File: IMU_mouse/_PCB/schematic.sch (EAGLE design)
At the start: 43 parts, among them IC1 REG1117, M1 WIRELESS-NRF24L01, U1 GY-521MPU6050

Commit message: IMU mouse PCB update
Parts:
- removed C2, C3, NRF: (no value), rcl:CPOL-USE2.5-5
- removed C5, C7, NRF_2: (no value), rcl:C-EUC0805
- removed D1: (no value), SparkFun-LED:LED3MM
- removed J1, J3, J4, NRF_POW1: (no value), SparkFun-Connectors:CONN_02LOCK
- removed JP2, JP3, JP4, JP5, NRF_POW: JUMPER-SMT_2_NO_SILK, SparkFun-Jumpers:JUMPER-SMT_2_NO_SILK
- removed M1: WIRELESS-NRF24L01, diy-modules:WIRELESS-NRF24L01
- removed R2, R3, R4, R5: (no value), rcl:R-US_R0805
- added JP_L, JP_R: JUMPER-SMT_2_NC_TRACE_SILK, SparkFun-Jumpers:JUMPER-SMT_2_NC_TRACE_SILK
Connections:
- removed net N$5: B1.*6, M1.CSN
- removed net N$6: M1.VCC, NRF_POW.2, NRF_POW1.2
- net 3.3V: no longer NRF.+, NRF_2.1, NRF_POW.1, NRF_POW1.1
- net 5V: now also LEFT.2, RIGHT.2; no longer LEFT.1, RIGHT.1
- net GND: no longer M1.GND, NRF.-, NRF_2.2
- net N$1: now also J2.2, JP_L.2, LEFT.1; no longer B1.12(MISO), M1.MISO
- net N$2: now also J2.1, JP_R.2, RIGHT.1; no longer B1.11(MOSI), M1.MOSI
- net N$3: now also B1.*5, JP_R.1; no longer B1.13(SCK), M1.SCK
- net N$4: now also B1.*6, JP_L.1; no longer B1.7, M1.CE
- net N$8: now also JP_SDA.2; no longer JP_SDA.1
- net N$9: now also JP_SCL.2; no longer JP_SCL.1
- net SCL: now also JP_SCL.1; no longer JP_SCL.2
- net SDA: now also JP_SDA.1; no longer JP_SDA.2
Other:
- moved on the sheet: B1, C_5V, C_5V_1, GY-521, H1, H2, H3, H4, IC1, IN, IN_2, J2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

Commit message: IMU mouse PCB
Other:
- moved on the sheet: H1, H2, H3, H4
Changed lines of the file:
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@@
 <instance part="J6" gate="G$1" x="147.32" y="38.1"/>
 <instance part="SHIELD" gate="G$1" x="157.48" y="10.16"/>
-<instance part="H1" gate="G$1" x="241.3" y="25.4"/>
-<instance part="H2" gate="G$1" x="241.3" y="20.32"/>
-<instance part="H3" gate="G$1" x="241.3" y="15.24"/>
-<instance part="H4" gate="G$1" x="241.3" y="10.16"/>
+<instance part="H1" gate="G$1" x="195.58" y="99.06"/>
+<instance part="H2" gate="G$1" x="195.58" y="93.98"/>
+<instance part="H3" gate="G$1" x="195.58" y="88.9"/>
+<instance part="H4" gate="G$1" x="195.58" y="83.82"/>
 <instance part="JP_SCL" gate="G$1" x="76.2" y="132.08"/>
 <instance part="JP_SDA" gate="G$1" x="76.2" y="124.46"/>

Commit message: update
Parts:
- removed C_5V: (no value), rcl:CPOL-USE2.5-5
- added 3.3V: (no value), SparkFun-Connectors:CONN_03
- added GY521_2: (no value), SparkFun-Connectors:CONN_08"
- added GY_3.3V: 3.3V, SparkFun-Jumpers:JUMPER-SMT_2_NO_NO-SILK
- added GY_5V_DEFAULT: 5V, SparkFun-Jumpers:JUMPER-SMT_2_NC_TRACE_SILK
- added POWER: FEMALE 2x3, SparkFun-Connectors:CONN_03X2FEMALE
- added RESET1: MOMENTARY-SWITCH-SPST-PTH-6.0MM, SparkFun-Switches:MOMENTARY-SWITCH-SPST-PTH-6.0MM
- added RESET2: 6*3.5mm, SparkFun-Switches:MOMENTARY-SWITCH-SPST-SMD-6.0X3.5MM
- IN, OUT: value (none) -> 100nF
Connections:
- new net N$5: GY521_2.1, GY_3.3V.1, GY_5V_DEFAULT.1, U1.VCC
- new net N$6: B1.RESET, RESET1.1, RESET2.1
- net 3.3V: now also 3.3V.1, 3.3V.2, 3.3V.3, GY_3.3V.2
- net 5V: now also GY_5V_DEFAULT.2, POWER.1, POWER.3, POWER.5; no longer C_5V.+, LEFT.2, RIGHT.2, U1.VCC
- net GND: now also GY521_2.2, LEFT.2, POWER.2, POWER.4, POWER.6, RESET1.2, RESET2.2, RIGHT.2; no longer C_5V.-
- net N$10: now also GY521_2.8
- net N$11: now also GY521_2.7
- net N$12: now also GY521_2.6
- net N$13: now also GY521_2.5
- net SCL: now also GY521_2.3
- net SDA: now also GY521_2.4
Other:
- moved on the sheet: GY-521, JP_SCL, JP_SDA

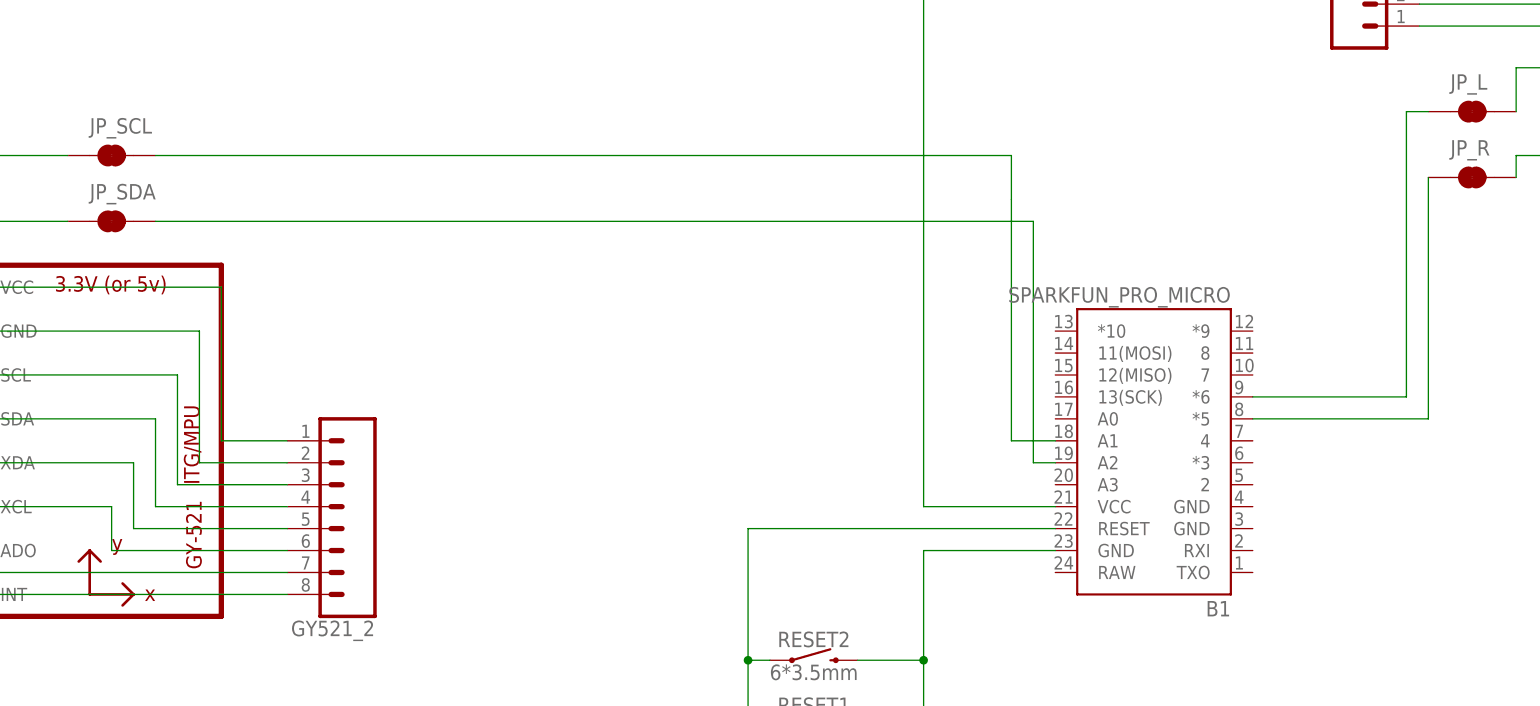
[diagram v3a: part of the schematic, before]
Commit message: IMU code, PCB update
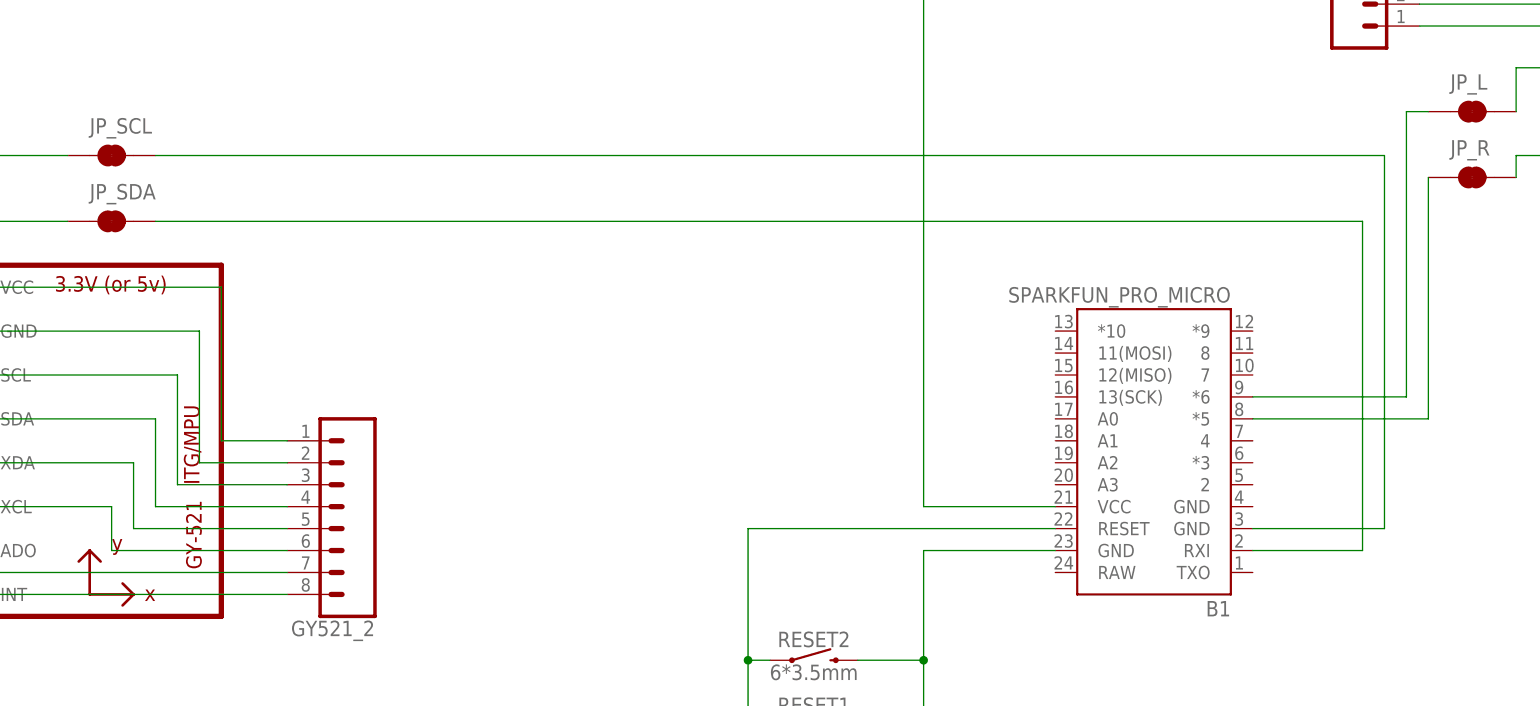
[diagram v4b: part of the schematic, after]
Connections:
- net N$8: now also B1.RXI; no longer B1.A2
- net N$9: now also B1.GND@1; no longer B1.A1
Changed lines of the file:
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@@
 <net name="N$8" class="0">
 <segment>
-<pinref part="B1" gate="G$1" pin="A2"/>
-<wire x1="132.08" y1="96.52" x2="129.54" y2="96.52" width="0.1524" layer="91"/>
-<wire x1="129.54" y1="96.52" x2="129.54" y2="124.46" width="0.1524" layer="91"/>
 <pinref part="JP_SDA" gate="G$1" pin="2"/>
-<wire x1="129.54" y1="124.46" x2="27.94" y2="124.46" width="0.1524" layer="91"/>
+<wire x1="167.64" y1="124.46" x2="27.94" y2="124.46" width="0.1524" layer="91"/>
+<pinref part="B1" gate="G$1" pin="RXI"/>
+<wire x1="154.94" y1="86.36" x2="167.64" y2="86.36" width="0.1524" layer="91"/>
+<wire x1="167.64" y1="86.36" x2="167.64" y2="124.46" width="0.1524" layer="91"/>
 </segment>
 </net>
 <net name="N$9" class="0">
 <segment>
-<pinref part="B1" gate="G$1" pin="A1"/>
-<wire x1="127" y1="127" x2="127" y2="99.06" width="0.1524" layer="91"/>
-<wire x1="127" y1="99.06" x2="132.08" y2="99.06" width="0.1524" layer="91"/>
-<wire x1="127" y1="132.08" x2="127" y2="127" width="0.1524" layer="91"/>
 <pinref part="JP_SCL" gate="G$1" pin="2"/>
-<wire x1="27.94" y1="132.08" x2="127" y2="132.08" width="0.1524" layer="91"/>
+<wire x1="27.94" y1="132.08" x2="170.18" y2="132.08" width="0.1524" layer="91"/>
+<wire x1="170.18" y1="132.08" x2="170.18" y2="88.9" width="0.1524" layer="91"/>
+<pinref part="B1" gate="G$1" pin="GND@1"/>
+<wire x1="170.18" y1="88.9" x2="154.94" y2="88.9" width="0.1524" layer="91"/>
 </segment>
 </net>

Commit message: IMU mouse update
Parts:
- B1: value SPARKFUN_PRO_MICRO -> ARDUINO_PRO_MICRO
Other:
- moved on the sheet: 3.3V, B1, C_5V_1, GY-521, GY521_2, GY_3.3V, GY_5V_DEFAULT, H1, H2, H3, H4, IC1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
